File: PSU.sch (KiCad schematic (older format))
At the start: 45 parts, among them J10 1053091202, Q5 BSS84PH6327XTSA2, Q6 IRF7416TRPBF, U13 AP62301WU-7, U14 AP62301WU-7, U15 AP62301WU-7, U16 LMV431IM5, U17 AP62301WU-7

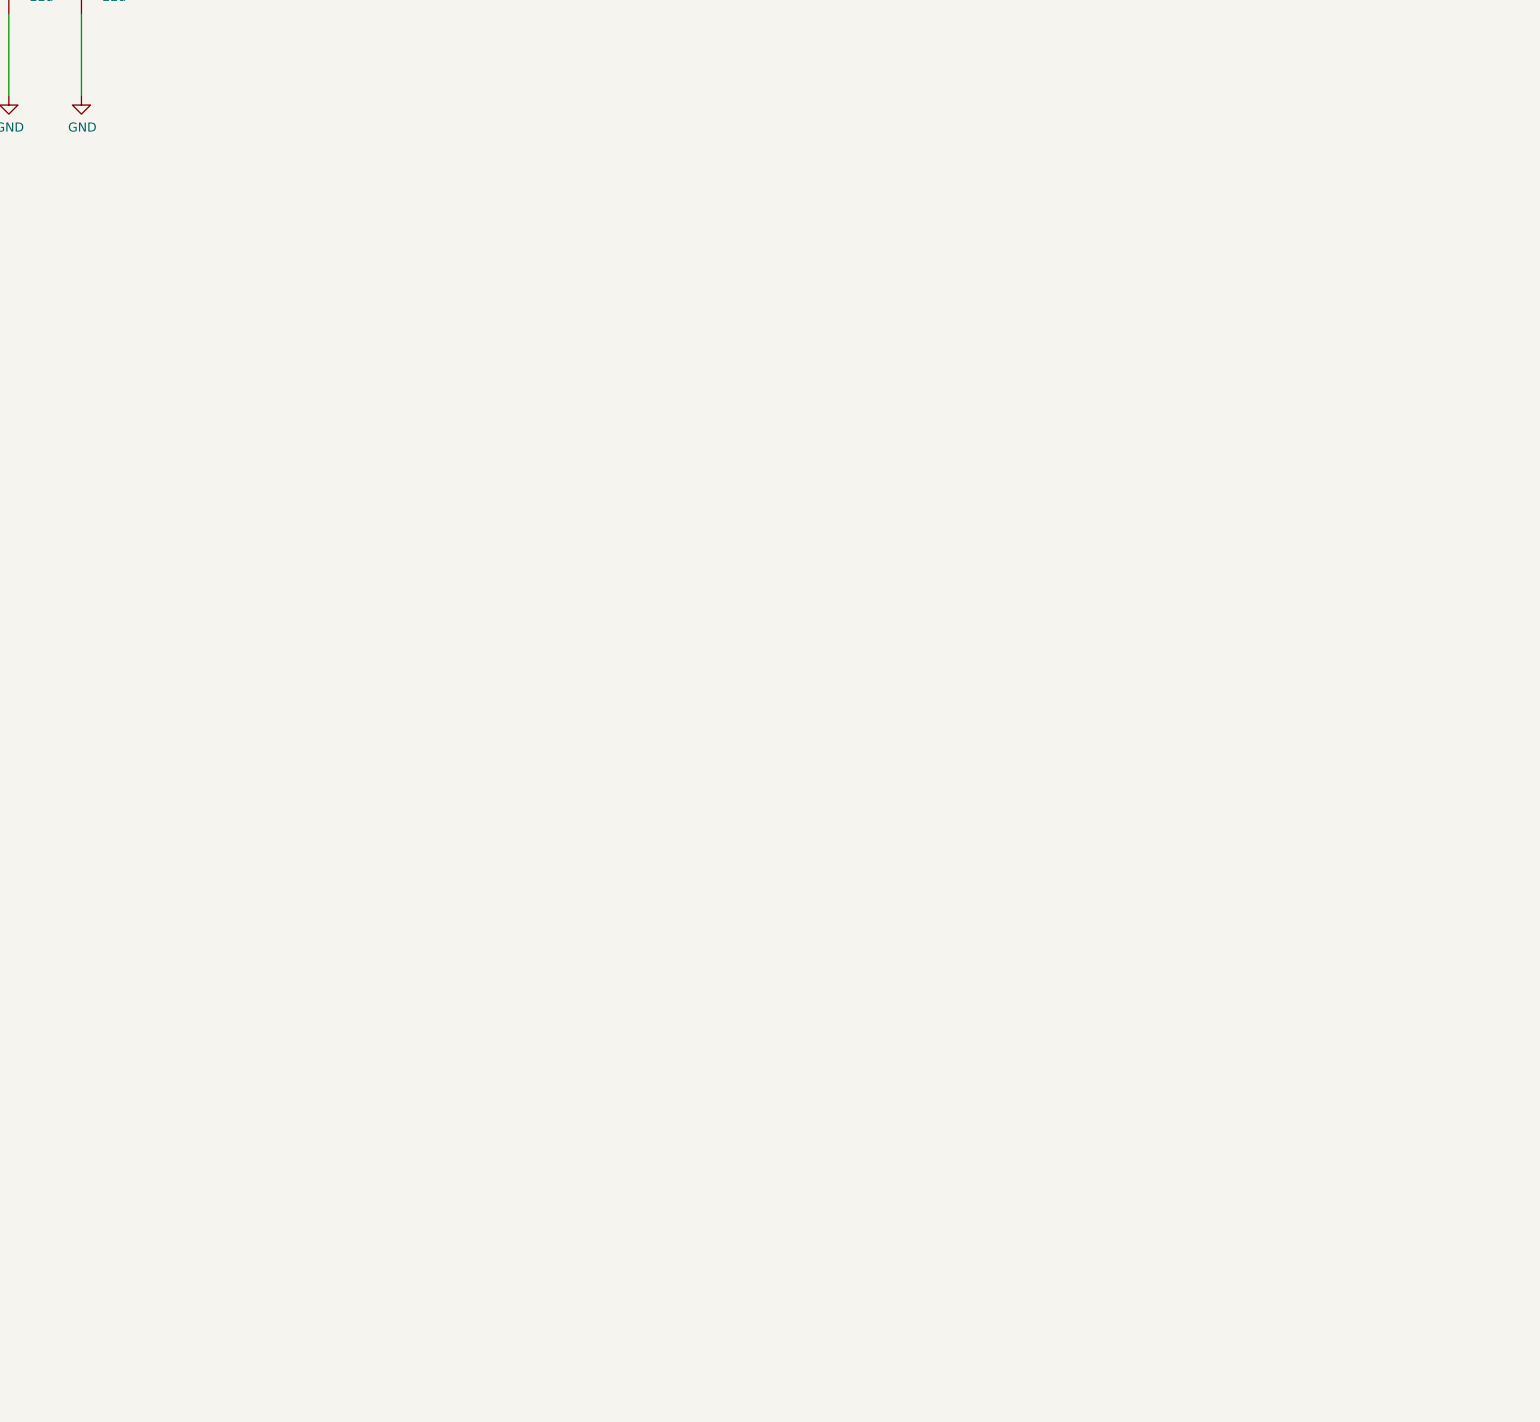
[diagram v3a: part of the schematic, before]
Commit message: add initial version of power management circuit
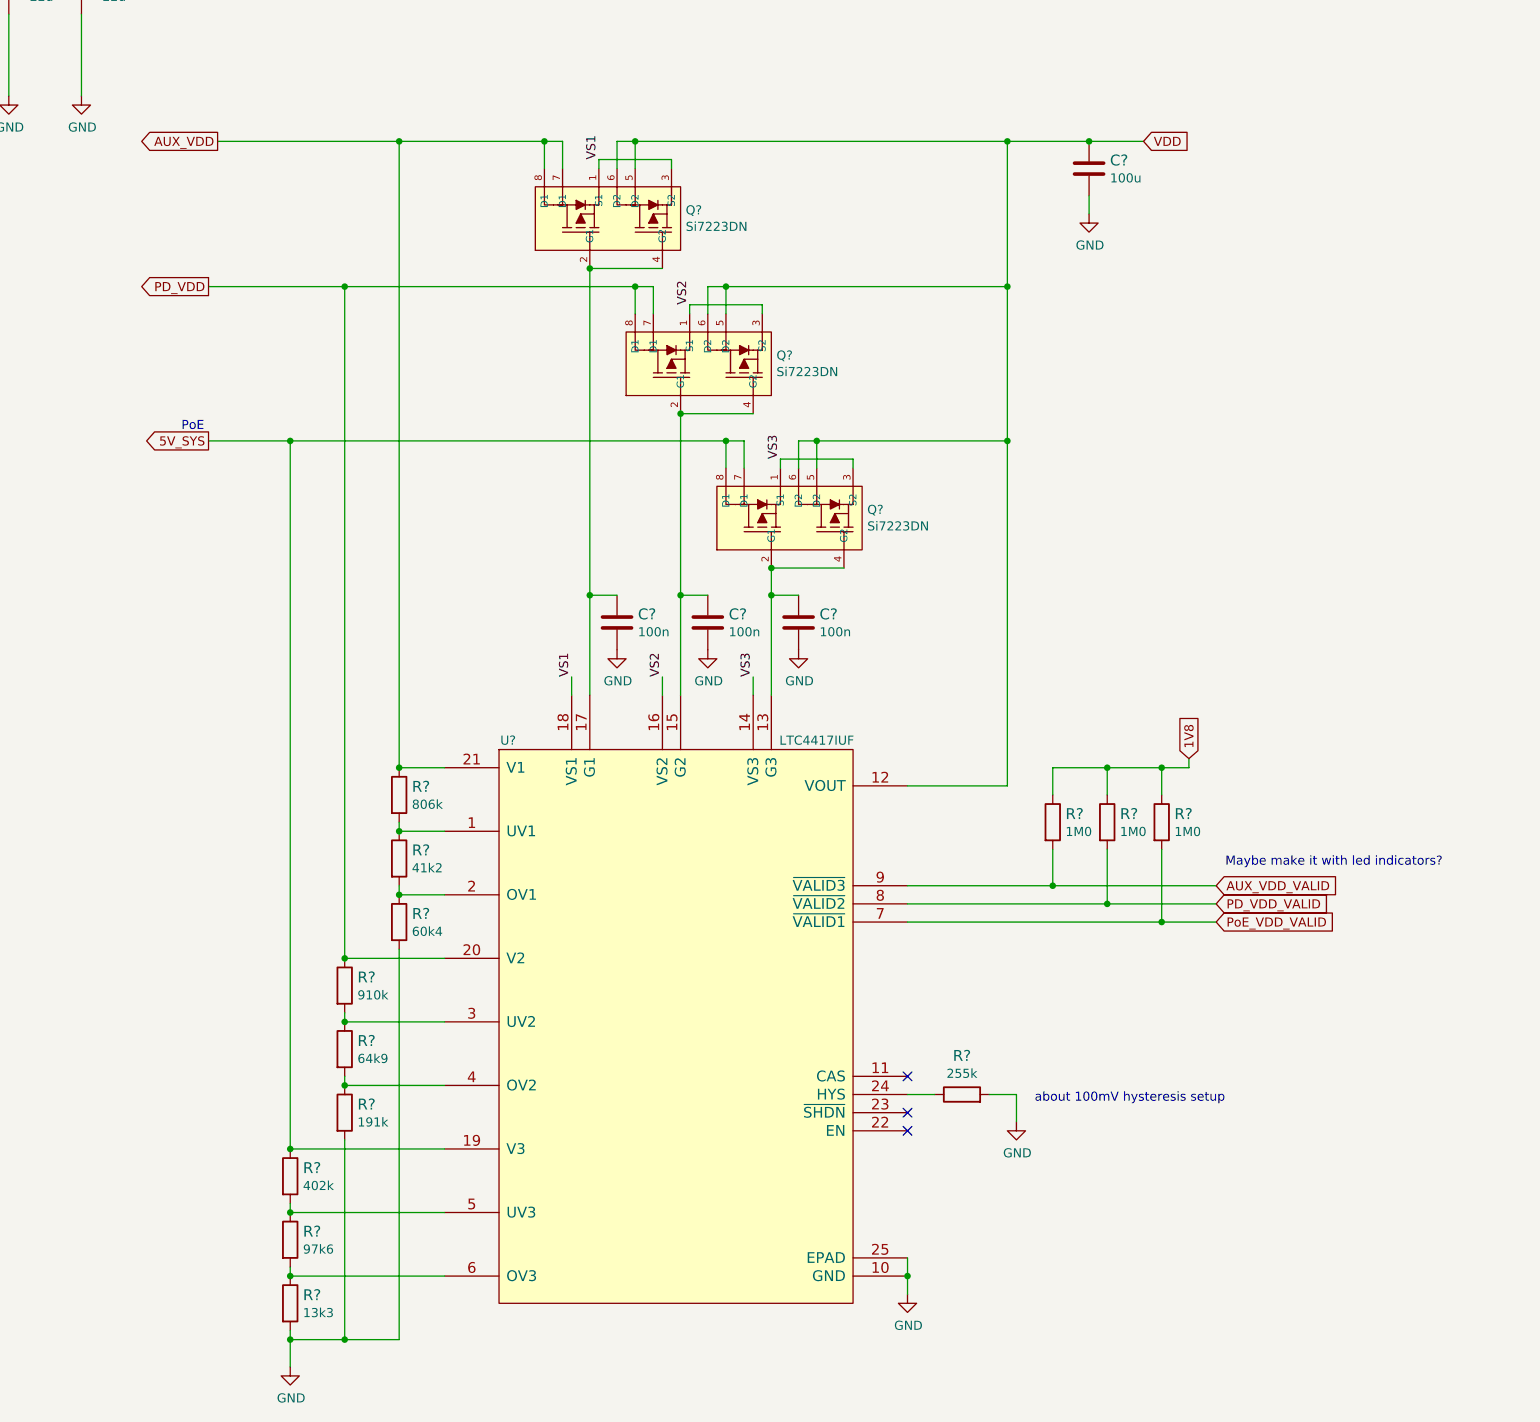
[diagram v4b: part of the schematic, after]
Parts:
- added C?: C_100u_0805, antmicro-footprints:0805-cap, symbol antmicroCapacitorsmisc:C_100u_0805
- added C? (x3): C_100n_0402, antmicro-footprints:0402-cap, symbol antmicroCapacitors0402:C_100n_0402
- added Q? (x3): Si7223DN, antmicro-footprints:PowerPak-1212, symbol antmicroTransistorsFETsMOSFETsArrays:Si7223DN
- added R? (x3): R_1M0_0402, antmicro-footprints:0402-res, symbol antmicroResistors0402:R_1M0_0402
- added R?: R_806k_0402, antmicro-footprints:0402-res, symbol antmicroResistors0402:R_806k_0402
- added R?: R_41k2_0402, antmicro-footprints:0402-res, symbol antmicroResistors0402:R_41k2_0402
- added R?: R_60k4_0402, antmicro-footprints:0402-res, symbol antmicroResistors0402:R_60k4_0402
- added R?: R_255k_0402, antmicro-footprints:0402-res, symbol antmicroResistors0402:R_255k_0402
- added R?: R_910k_0402, antmicro-footprints:0402-res, symbol antmicroResistors0402:R_910k_0402
- added R?: R_64k9_0402, antmicro-footprints:0402-res, symbol antmicroResistors0402:R_64k9_0402
- added R?: R_191k_0402, antmicro-footprints:0402-res, symbol antmicroResistors0402:R_191k_0402
- added R?: R_402k_0402, antmicro-footprints:0402-res, symbol antmicroResistors0402:R_402k_0402
- added R?: R_97k6_0402, antmicro-footprints:0402-res, symbol antmicroResistors0402:R_97k6_0402
- added R?: R_13k3_0402, antmicro-footprints:0402-res, symbol antmicroResistors0402:R_13k3_0402
- added U?: LTC4417IUF, antmicro-footprints:LTC4417IUF-TRPBF, symbol antmicroPMICPowerDistributionSwitchesLoadDrivers:LTC4417IUF
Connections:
- net labels added: 1V8, AUX_VDD_VALID, PD_VDD_VALID, PoE_VDD_VALID, VDD, VS1, VS2, VS3
- wire segments 132 -> 235
- no-connect marks 0 -> 3
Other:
- note added: "Maybe make it with led indicators?\n"
- note added: "PoE\n"
- note added: "about 100mV hysteresis setup"

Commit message: Fix naming in power labels
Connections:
- net 5V is gone; now on net VDD: C11.1, C13.1, C9.1, U13.3 (VIN), U14.3 (VIN), U15.3 (VIN)
- net 5V_SYS: no longer Q?.7 (D1), Q?.8 (D1), R?.1, U?.19 (V3)
- net VDD: now also C109.1, Q5.3 (S), Q6.1, Q6.2, Q6.3, R91.1, R93.1, U17.3 (VIN)
- new net 5V_POE: Q?.7 (D1), Q?.8 (D1), R?.1, U?.19 (V3)
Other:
- note removed: "PoE\n"
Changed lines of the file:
@@
 Connection ~ 5850 1900
 Wire Wire Line
-	7500 2100 7700 2100
+	7500 2100 7775 2100
 Text Notes 6400 1400 0    50   ~ 0
 Bypass transistor
@@
 	1    0    0    -1
 $EndComp
-Text GLabel 7700 2100 2    50   Input ~ 0
+Text GLabel 7850 2100 2    50   Output ~ 0
 5V_SYS
 $Comp
@@
 	9050 3000 9500 3000
 Connection ~ 9050 3000
-Text GLabel 9500 3000 2    50   Input ~ 0
+Text GLabel 9500 3000 2    50   Output ~ 0
 5V_SYS
 Wire Wire Line
@@
 Wire Wire Line
 	3150 9575 3550 9575
-Text GLabel 1725 9575 0    50   Input ~ 0
-5V
 Wire Wire Line
 	5150 9575 5300 9575
@@
 Wire Wire Line
 	3150 7925 3550 7925
-Text GLabel 1725 7925 0    50   Input ~ 0
-5V
 Wire Wire Line
 	5150 7925 5300 7925
@@
 Wire Wire Line
 	3150 6150 3550 6150
-Text GLabel 1725 6150 0    50   Input ~ 0
-5V
 Text GLabel 5300 7925 2    50   Input ~ 0
 1V8_SYS
@@
 Wire Wire Line
 	1625 4575 1750 4575
-Text GLabel 1000 1225 0    50   Input ~ 0
-AUX_VDD
-Text GLabel 1000 1000 0    50   Input ~ 0
-PD_VDD
 $Comp
 L antmicroPMICPowerDistributionSwitchesLoadDrivers:LTC4417IUF U?
@@
 	13100 5900 13100 5750
 Connection ~ 13100 5750
-Text GLabel 9800 4100 0    50   Output ~ 0
+Text GLabel 9800 4100 0    50   Input ~ 0
 AUX_VDD
 Text GLabel 9750 4900 0    50   Output ~ 0
@@
 	14150 4100 14600 4100
 Connection ~ 14150 4100
-Text GLabel 14900 4100 2    50   Input ~ 0
+Text GLabel 14900 4100 2    50   Output ~ 0
 VDD
-Text Notes 9600 5700 0    50   ~ 0
-PoE\n
 $Comp
 L antmicroCapacitorsmisc:C_100u_0805 C?
@@
 U 1 1 6230B5B4
 P 14600 4500
+AR Path="/6230B5B4" Ref="#PWR?"  Part="1"
+AR Path="/61B0DC30/6230B5B4" Ref="#PWR?"  Part="1"
 F 0 "#PWR?" H 14600 4250 50  0001 C CNN
 F 1 "GND" H 14605 4327 50  0000 C CNN
@@
 U 1 1 6231D12F
 P 13600 10450
+AR Path="/6231D12F" Ref="#PWR?"  Part="1"
+AR Path="/61B0DC30/6231D12F" Ref="#PWR?"  Part="1"
 F 0 "#PWR?" H 13600 10200 50  0001 C CNN
 F 1 "GND" H 13605 10277 50  0000 C CNN
@@
 U 1 1 62350588
 P 12000 6900
+AR Path="/62350588" Ref="#PWR?"  Part="1"
+AR Path="/61B0DC30/62350588" Ref="#PWR?"  Part="1"
 F 0 "#PWR?" H 12000 6650 50  0001 C CNN
 F 1 "GND" H 12005 6727 50  0000 C CNN
@@
 U 1 1 62350892
 P 12500 6900
+AR Path="/62350892" Ref="#PWR?"  Part="1"
+AR Path="/61B0DC30/62350892" Ref="#PWR?"  Part="1"
 F 0 "#PWR?" H 12500 6650 50  0001 C CNN
 F 1 "GND" H 12505 6727 50  0000 C CNN
@@
 U 1 1 62350BDA
 P 13000 6900
+AR Path="/62350BDA" Ref="#PWR?"  Part="1"
+AR Path="/61B0DC30/62350BDA" Ref="#PWR?"  Part="1"
 F 0 "#PWR?" H 13000 6650 50  0001 C CNN
 F 1 "GND" H 13005 6727 50  0000 C CNN
@@
 U 1 1 6245617E
 P 14200 9500
+AR Path="/6245617E" Ref="#PWR?"  Part="1"
+AR Path="/61B0DC30/6245617E" Ref="#PWR?"  Part="1"
 F 0 "#PWR?" H 14200 9250 50  0001 C CNN
 F 1 "GND" H 14205 9327 50  0000 C CNN
@@
 U 1 1 625AC652
 P 10200 10850
+AR Path="/625AC652" Ref="#PWR?"  Part="1"
+AR Path="/61B0DC30/625AC652" Ref="#PWR?"  Part="1"
 F 0 "#PWR?" H 10200 10600 50  0001 C CNN
 F 1 "GND" H 10205 10677 50  0000 C CNN
@@
 Wire Wire Line
 	10800 4100 11600 4100
-Text GLabel 9750 5750 0    50   Output ~ 0
-5V_SYS
+Text GLabel 9750 5750 0    50   Input ~ 0
+5V_POE
 Wire Wire Line
 	9750 5750 10200 5750
@@
 NoConn ~ 13600 9450
 NoConn ~ 13600 9250
+Text GLabel 1200 1100 0    50   Input ~ 0
+VDD
+Text GLabel 1425 6725 0    50   Input ~ 0
+VDD
+Text GLabel 1725 6150 0    50   Input ~ 0
+VDD
+Text GLabel 1725 7925 0    50   Input ~ 0
+VDD
+Text GLabel 1725 9575 0    50   Input ~ 0
+VDD
+$Comp
+L sa800u-baseboard-hw:PWR_FLAG #FLG?
+U 1 1 61F11F38
+P 7775 2100
+AR Path="/61B0DC30/61F11F38" Ref="#FLG?"  Part="1"
+AR Path="/61DC2BE0/61F11F38" Ref="#FLG?"  Part="1"
+F 0 "#FLG?" H 7775 2175 50  0001 C CNN
+F 1 "PWR_FLAG" H 7775 2273 50  0000 C CNN
+F 2 "" H 7775 2100 50  0001 C CNN
+F 3 "~" H 7775 2100 50  0001 C CNN
+	1    7775 2100
+	1    0    0    -1
+$EndComp
+Connection ~ 7775 2100
+Wire Wire Line
+	7775 2100 7850 2100
+$Comp
+L sa800u-baseboard-hw:PWR_FLAG #FLG?
+U 1 1 61F3C00C
+P 9050 3000
+AR Path="/61B0DC30/61F3C00C" Ref="#FLG?"  Part="1"
+AR Path="/61DC2BE0/61F3C00C" Ref="#FLG?"  Part="1"
+F 0 "#FLG?" H 9050 3075 50  0001 C CNN
+F 1 "PWR_FLAG" H 9050 3173 50  0000 C CNN
+F 2 "" H 9050 3000 50  0001 C CNN
+F 3 "~" H 9050 3000 50  0001 C CNN
+	1    9050 3000
+	1    0    0    -1
+$EndComp
+$Comp
+L sa800u-baseboard-hw:PWR_FLAG #FLG?
+U 1 1 61F4D0A9
+P 14150 4100
+AR Path="/61B0DC30/61F4D0A9" Ref="#FLG?"  Part="1"
+AR Path="/61DC2BE0/61F4D0A9" Ref="#FLG?"  Part="1"
+F 0 "#FLG?" H 14150 4175 50  0001 C CNN
+F 1 "PWR_FLAG" H 14150 4273 50  0000 C CNN
+F 2 "" H 14150 4100 50  0001 C CNN
+F 3 "~" H 14150 4100 50  0001 C CNN
+	1    14150 4100
+	1    0    0    -1
+$EndComp
 $EndSCHEMATC

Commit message: Loclib
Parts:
- C?: footprint antmicro-footprints:0805-cap -> sa800u-baseboard-hw-footprints:0805-cap; symbol antmicroCapacitorsmisc:C_100u_0805 -> sa800u-baseboard-hw:C_100u_0805
- C? (x3): footprint antmicro-footprints:0402-cap -> sa800u-baseboard-hw-footprints:0402-cap; symbol antmicroCapacitors0402:C_100n_0402 -> sa800u-baseboard-hw:C_100n_0402
- Q? (x3): footprint antmicro-footprints:PowerPak-1212 -> sa800u-baseboard-hw-footprints:PowerPak-1212; symbol antmicroTransistorsFETsMOSFETsArrays:Si7223DN -> sa800u-baseboard-hw:Si7223DN
- R? (x3): footprint antmicro-footprints:0402-res -> sa800u-baseboard-hw-footprints:0402-res; symbol antmicroResistors0402:R_1M0_0402 -> sa800u-baseboard-hw:R_1M0_0402
- R?: footprint antmicro-footprints:0402-res -> sa800u-baseboard-hw-footprints:0402-res; symbol antmicroResistors0402:R_806k_0402 -> sa800u-baseboard-hw:R_806k_0402
- R?: footprint antmicro-footprints:0402-res -> sa800u-baseboard-hw-footprints:0402-res; symbol antmicroResistors0402:R_41k2_0402 -> sa800u-baseboard-hw:R_41k2_0402
- R?: footprint antmicro-footprints:0402-res -> sa800u-baseboard-hw-footprints:0402-res; symbol antmicroResistors0402:R_60k4_0402 -> sa800u-baseboard-hw:R_60k4_0402
- R?: footprint antmicro-footprints:0402-res -> sa800u-baseboard-hw-footprints:0402-res; symbol antmicroResistors0402:R_255k_0402 -> sa800u-baseboard-hw:R_255k_0402
- R?: footprint antmicro-footprints:0402-res -> sa800u-baseboard-hw-footprints:0402-res; symbol antmicroResistors0402:R_910k_0402 -> sa800u-baseboard-hw:R_910k_0402
- R?: footprint antmicro-footprints:0402-res -> sa800u-baseboard-hw-footprints:0402-res; symbol antmicroResistors0402:R_64k9_0402 -> sa800u-baseboard-hw:R_64k9_0402
- R?: footprint antmicro-footprints:0402-res -> sa800u-baseboard-hw-footprints:0402-res; symbol antmicroResistors0402:R_191k_0402 -> sa800u-baseboard-hw:R_191k_0402
- R?: footprint antmicro-footprints:0402-res -> sa800u-baseboard-hw-footprints:0402-res; symbol antmicroResistors0402:R_402k_0402 -> sa800u-baseboard-hw:R_402k_0402
- R?: footprint antmicro-footprints:0402-res -> sa800u-baseboard-hw-footprints:0402-res; symbol antmicroResistors0402:R_97k6_0402 -> sa800u-baseboard-hw:R_97k6_0402
- R?: footprint antmicro-footprints:0402-res -> sa800u-baseboard-hw-footprints:0402-res; symbol antmicroResistors0402:R_13k3_0402 -> sa800u-baseboard-hw:R_13k3_0402
- U?: footprint antmicro-footprints:LTC4417IUF-TRPBF -> sa800u-baseboard-hw-footprints:LTC4417IUF-TRPBF; symbol antmicroPMICPowerDistributionSwitchesLoadDrivers:LTC4417IUF -> sa800u-baseboard-hw:LTC4417IUF
